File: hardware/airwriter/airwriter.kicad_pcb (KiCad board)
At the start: 30 x 45 mm, 4 parts

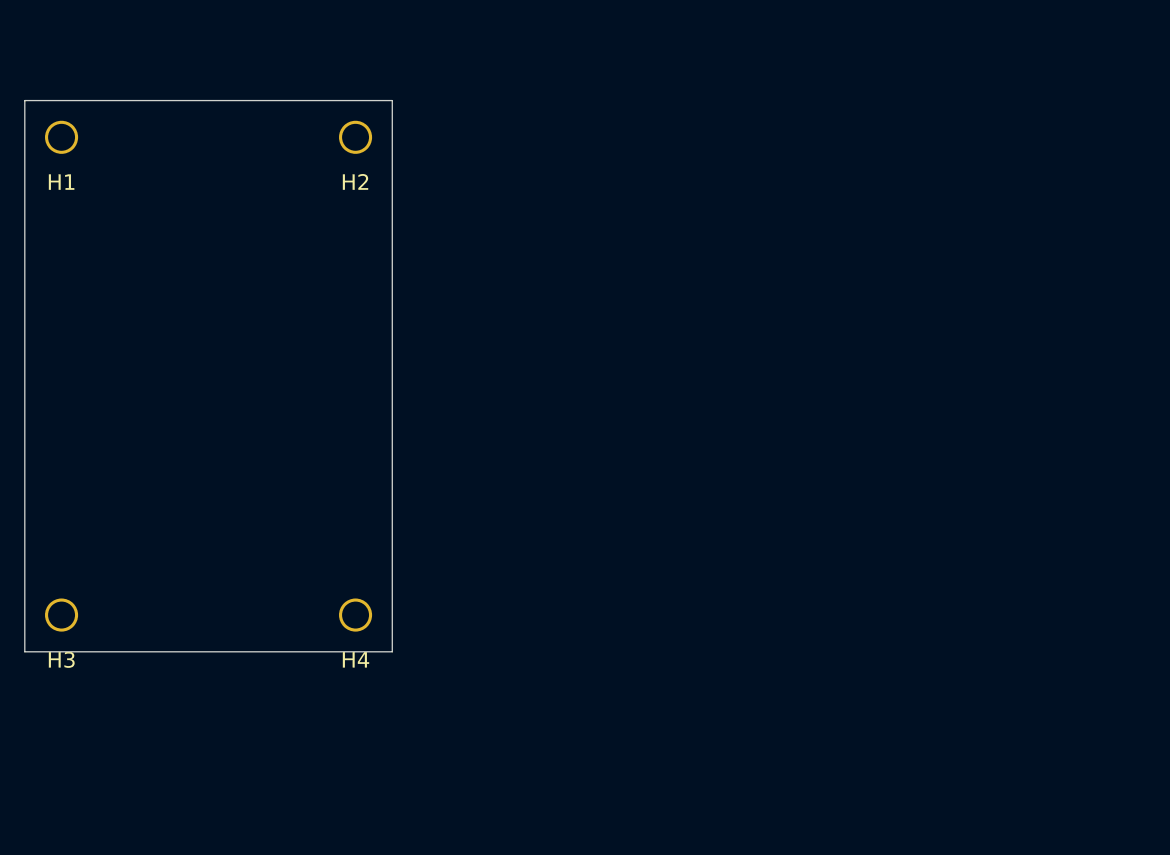
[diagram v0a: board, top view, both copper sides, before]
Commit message: Import footprints to the board; fix malformed mini-DIN footprint
F8 pulled in 35 of 37 parts. The two it dropped, and why:

- R9 had no footprint assigned. It was added to the schematic after the batch
  that set footprints, so it never got one. Assigned R_0603.
- J2 was skipped because the generated .kicad_mod carried unescaped double
  quotes inside its (descr ...) string, which makes the s-expression malformed.
  KiCad failed to load the footprint and dropped the part silently. Rewrote the
  descr and added a balance check.

Both are now on the board with their nets, injected directly rather than
costing another GUI round trip. 41 footprints total, board loads clean.

Project library tables switched from absolute paths to ${KIPRJMOD} so they
travel with the repo.

DRC currently reports 20 violations and 98 unconnected — expected, nothing is
placed or routed yet.

Refs: W-568
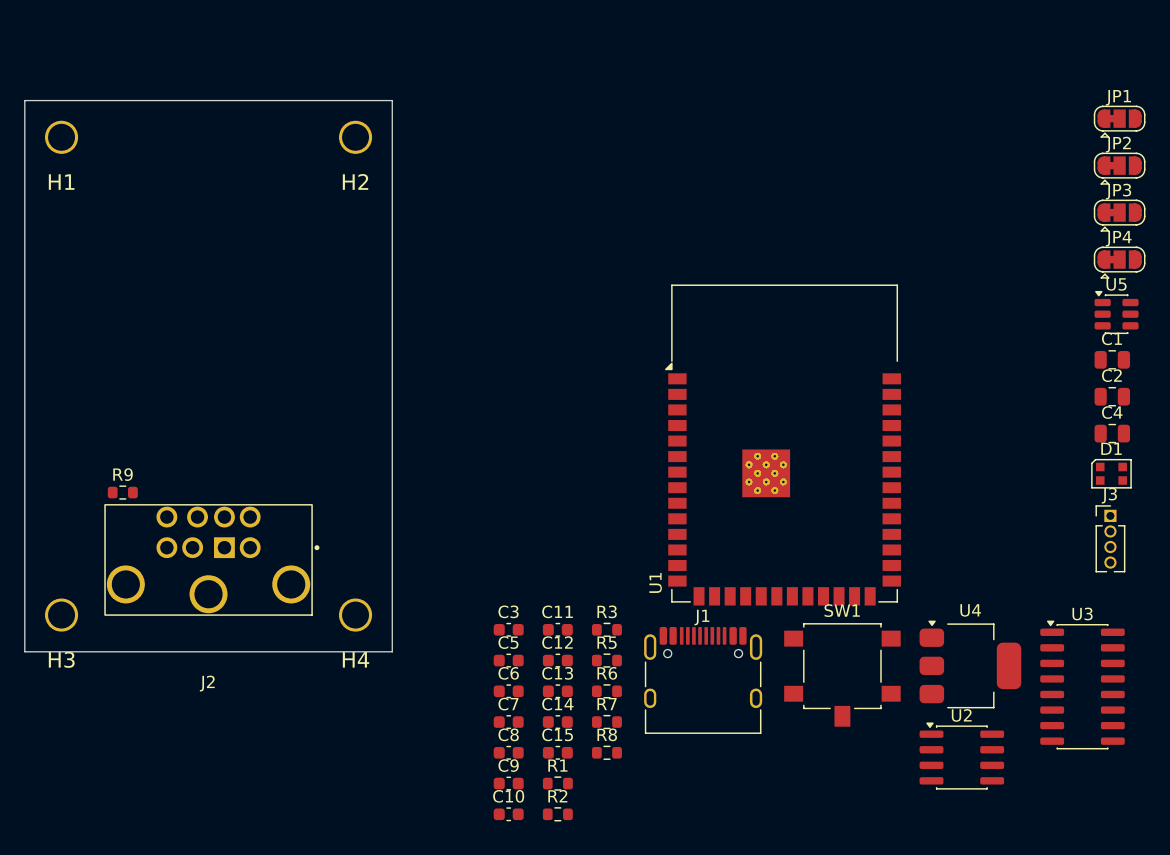
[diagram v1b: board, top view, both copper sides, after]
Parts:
- added C1: 22u, Capacitor_SMD:C_0805_2012Metric, F.Cu at (188.8, 81.2)
- added C10: 100n, Capacitor_SMD:C_0603_1608Metric, F.Cu at (139.5, 118.3)
- added C11: 100n, Capacitor_SMD:C_0603_1608Metric, F.Cu at (143.5, 103.2)
- added C12: 100n, Capacitor_SMD:C_0603_1608Metric, F.Cu at (143.5, 105.7)
- added C13: 100n, Capacitor_SMD:C_0603_1608Metric, F.Cu at (143.5, 108.2)
- added C14: 100n, Capacitor_SMD:C_0603_1608Metric, F.Cu at (143.5, 110.7)
- added C15: 1n, Capacitor_SMD:C_0603_1608Metric, F.Cu at (143.5, 113.2)
- added C2: 10u, Capacitor_SMD:C_0805_2012Metric, F.Cu at (188.8, 84.2)
- added C3: 100n, Capacitor_SMD:C_0603_1608Metric, F.Cu at (139.5, 103.2)
- added C4: 10u, Capacitor_SMD:C_0805_2012Metric, F.Cu at (188.8, 87.2)
- added C5: 100n, Capacitor_SMD:C_0603_1608Metric, F.Cu at (139.5, 105.7)
- added C6: 1u, Capacitor_SMD:C_0603_1608Metric, F.Cu at (139.5, 108.2)
- added C7: 100n, Capacitor_SMD:C_0603_1608Metric, F.Cu at (139.5, 110.7)
- added C8: 100n, Capacitor_SMD:C_0603_1608Metric, F.Cu at (139.5, 113.2)
- added C9: 100n, Capacitor_SMD:C_0603_1608Metric, F.Cu at (139.5, 115.8)
- added D1: WS2812B-2020, LED_SMD:LED_WS2812B-2020_PLCC4_2.0x2.0mm, F.Cu at (188.7, 90.5)
- added J1: USB-C 5V in, Connector_USB:USB_C_Receptacle_HRO_TYPE-C-31-M-12, F.Cu at (155.4, 107.7)
- added J2: Mini-DIN-8 to printer, airwriter:MiniDIN-8_Kycon_KMDGX-8S-BS_RightAngle, F.Cu at (115.0, 105.0)
- added J3: Bring-up USB/UART, Connector_PinHeader_1.27mm:PinHeader_1x04_P1.27mm_Vertical, F.Cu at (188.6, 93.9)
- added JP1: RxD+ pol, Jumper:SolderJumper-3_P1.3mm_Bridged12_RoundedPad1.0x1.5mm, F.Cu at (189.4, 61.5)
- added JP2: RxD- pol, Jumper:SolderJumper-3_P1.3mm_Bridged12_RoundedPad1.0x1.5mm, F.Cu at (189.4, 65.3)
- added JP3: TxD- pol, Jumper:SolderJumper-3_P1.3mm_Bridged12_RoundedPad1.0x1.5mm, F.Cu at (189.4, 69.1)
- added JP4: TxD+ pol, Jumper:SolderJumper-3_P1.3mm_Bridged12_RoundedPad1.0x1.5mm, F.Cu at (189.4, 73.0)
- added R1: 5.1k, Resistor_SMD:R_0603_1608Metric, F.Cu at (143.5, 115.8)
- added R2: 5.1k, Resistor_SMD:R_0603_1608Metric, F.Cu at (143.5, 118.3)
- added R3: 10k, Resistor_SMD:R_0603_1608Metric, F.Cu at (147.5, 103.2)
- added R5: 120R DNP, Resistor_SMD:R_0603_1608Metric, F.Cu at (147.5, 105.7)
- added R6: 4.7k DNP, Resistor_SMD:R_0603_1608Metric, F.Cu at (147.5, 108.2)
- added R7: 4.7k DNP, Resistor_SMD:R_0603_1608Metric, F.Cu at (147.5, 110.7)
- added R8: 0R, Resistor_SMD:R_0603_1608Metric, F.Cu at (147.5, 113.2)
- added R9: 0R DNP, Resistor_SMD:R_0603_1608Metric, F.Cu at (108.0, 92.0)
- added SW1: CONFIG/BOOT, Button_Switch_SMD:SW_SPST_B3S-1100, F.Cu at (166.7, 107.1)
- added U1: ESP32-S3-WROOM-1-N8R2, RF_Module:ESP32-S3-WROOM-1, F.Cu at (162.0, 88.0)
- added U2: MAX3490ESA+, Package_SO:SOIC-8_3.9x4.9mm_P1.27mm, F.Cu at (176.5, 113.6)
- added U3: MAX3232ESE+, Package_SO:SOIC-16_3.9x9.9mm_P1.27mm, F.Cu at (186.3, 107.8)
- added U4: AP7361C-33E, Package_TO_SOT_SMD:SOT-223-3_TabPin2, F.Cu at (177.2, 106.2)
- added U5: USBLC6-2SC6, Package_TO_SOT_SMD:SOT-23-6, F.Cu at (189.1, 77.4)
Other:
- copper layers 0 -> 2

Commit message: Place the board; clear every DRC error except silkscreen
Board is 32 x 54mm (1728 sq mm) against the spec's 55 x 35 (1925). The floor is
set by three parts that cannot move: the WROOM-1 needs 18 x 19.5mm of board with
its antenna overhanging the top edge, and the mini-DIN body reserves the whole
bottom 13.5mm, with the USB-C receptacle beside it.

Placement was done against measured courtyard extents rather than datasheet
guesses, which caught two things worth noting:

- SW1's B3S-1100 footprint has a 10 x 8.9mm courtyard, much larger than the
  4.5mm tactile the spec assumed. It now sits in the pocket right of the DIN.
- The WROOM-1 courtyard is 48 x 41mm because it includes the antenna keepout.
  Courtyard checks against it are not meaningful; parts are kept clear of the
  18 x 25.5mm module body instead.

Fixes along the way:
- set_board_size appended a second outline rather than replacing the first, so
  the board had two overlapping rectangles. Removed the stale one.
- Design rules live in .kicad_pro in KiCad 10, not the board file. The MCP
  set_design_rules tool writes them into the .kicad_pcb setup block, which
  duplicated keys and made the board unloadable. Rules are now set in the
  project file, where DRC actually reads them.
- min_through_hole_diameter relaxed to 0.2mm: the WROOM-1 footprint uses 0.2mm
  thermal vias in its ground pad, which is within JLCPCB capability.
- Mounting holes renamed to the real stock MountingHole_2.2mm_M2 footprint.

DRC: 219 -> 82. The 75 silkscreen violations are reference-designator text
overlap, cleaned up at the end of layout. 98 unconnected items remain because
nothing is routed yet.

Refs: W-568
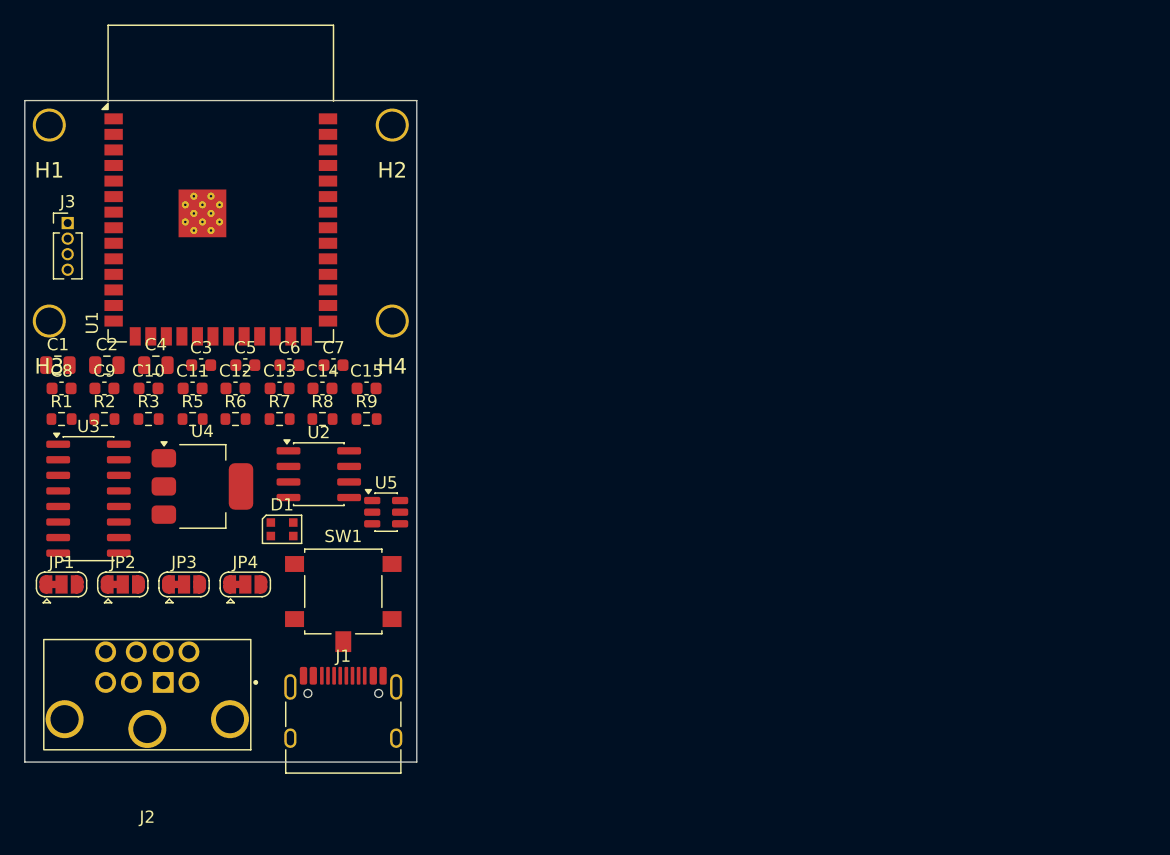
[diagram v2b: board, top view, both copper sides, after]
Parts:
- H1, H2, H3, H4: footprint MountingHole:MountingHole_2.2mm -> MountingHole:MountingHole_2.2mm_M2
- moved JP1 94.4 mm to (103.0, 99.5)
- moved J3 88.4 mm to (103.5, 70.0)
- moved JP2 88.3 mm to (108.0, 99.5)
- moved C1 86.1 mm to (102.7, 81.6)
- moved U3 82.6 mm to (105.2, 92.5)
- moved JP3 82.2 mm to (113.0, 99.5)
- moved C2 82.1 mm to (106.7, 81.6)
- moved C4 78.3 mm to (110.7, 81.6)
- moved JP4 76.1 mm to (118.0, 99.5)
- moved D1 67.9 mm to (121.0, 95.0)
- moved U4 64.4 mm to (114.5, 91.5)
- moved U5 61.8 mm to (129.5, 93.6)
- moved U2 57.4 mm to (124.0, 90.5)
- moved U1 50.7 mm to (116.0, 66.8)
- moved R1 50.3 mm to (103.0, 86.0)
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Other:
- board size 30 x 45 mm -> 32 x 54 mm

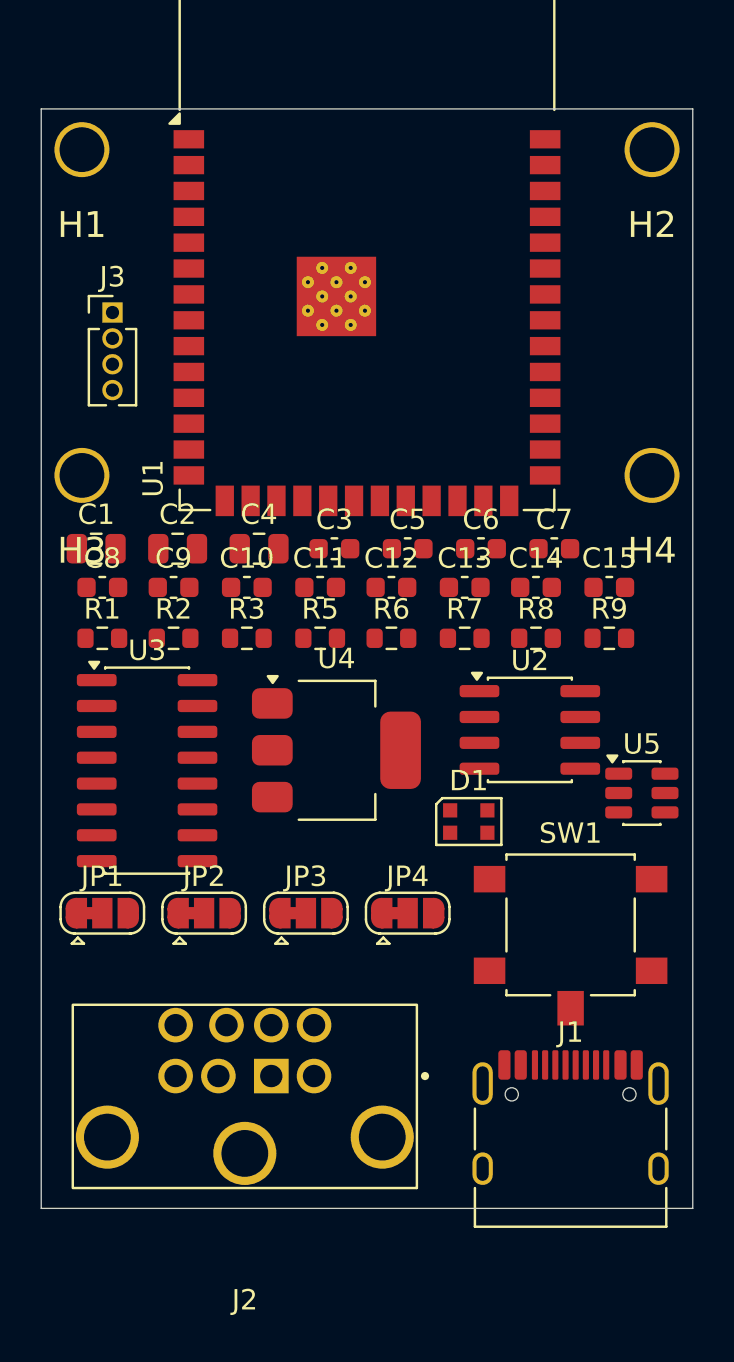
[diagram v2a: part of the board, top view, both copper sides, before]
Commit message: Finish placement: DRC down to 6 benign violations
- Swapped SW1 from B3S-1100 (10 x 8.9mm courtyard) to B3U-1000P (4.8 x 3.4mm).
  The big switch had become the binding constraint on the pocket beside the
  mini-DIN; the small one frees it entirely.
- Moved every reference designator from F.SilkS to F.Fab. At this density the
  silkscreen text was unreadable and generated 75 of the 82 violations. The
  designators still print on the assembly drawing.
- J2 carried both a legacy (fp_text reference "REF**") and a modern Reference
  property, so the render showed REF**. Stripped the legacy text from the board
  and the library module.
- J1 pulled back to sit flush with the board edge instead of overhanging 1.7mm.
- Mounting holes rebuilt from the real stock MountingHole_2.2mm_M2 footprint
  rather than the geometry the MCP tool invented.

Remaining 6 are accepted: H1/H2 sit inside the WROOM-1's antenna-keepout
courtyard (they are NPTH, no copper, so this is fine), the module's silkscreen
crosses the board edge where it deliberately overhangs, and two library
metadata mismatches on U1 and J2.

Still 98 unconnected — routing next.

Refs: W-568
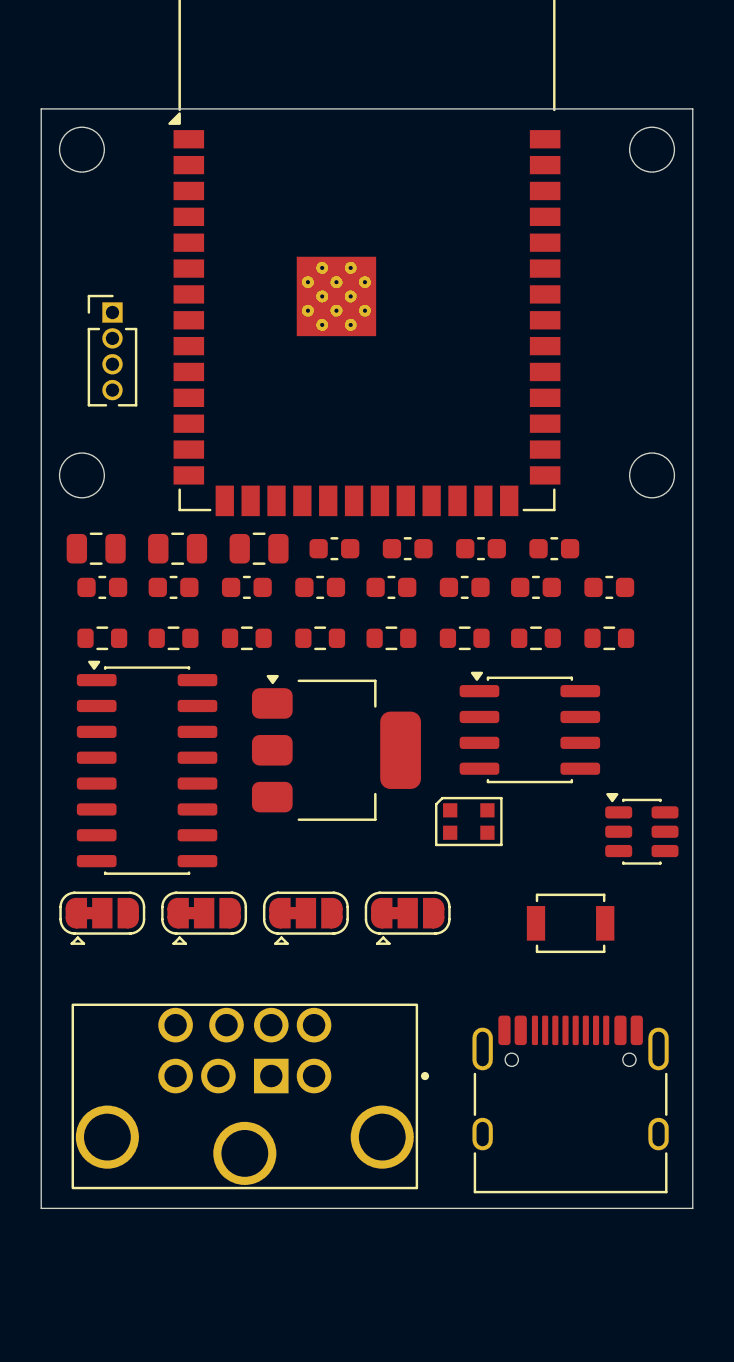
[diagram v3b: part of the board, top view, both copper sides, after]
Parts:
- H1, H2, H3, H4: value MountingHole -> MountingHole_2.2mm_M2
- SW1: value CONFIG/BOOT -> SW_SPST_B3U-1000P; footprint Button_Switch_SMD:SW_SPST_B3S-1100 -> Button_Switch_SMD:SW_SPST_B3U-1000P
- moved U5 1.90 mm to (129.5, 95.5)
- moved J1 1.70 mm to (126.0, 109.3)
- moved SW1 1.00 mm to (126.0, 100.0)
